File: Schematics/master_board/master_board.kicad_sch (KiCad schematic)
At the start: 9 parts

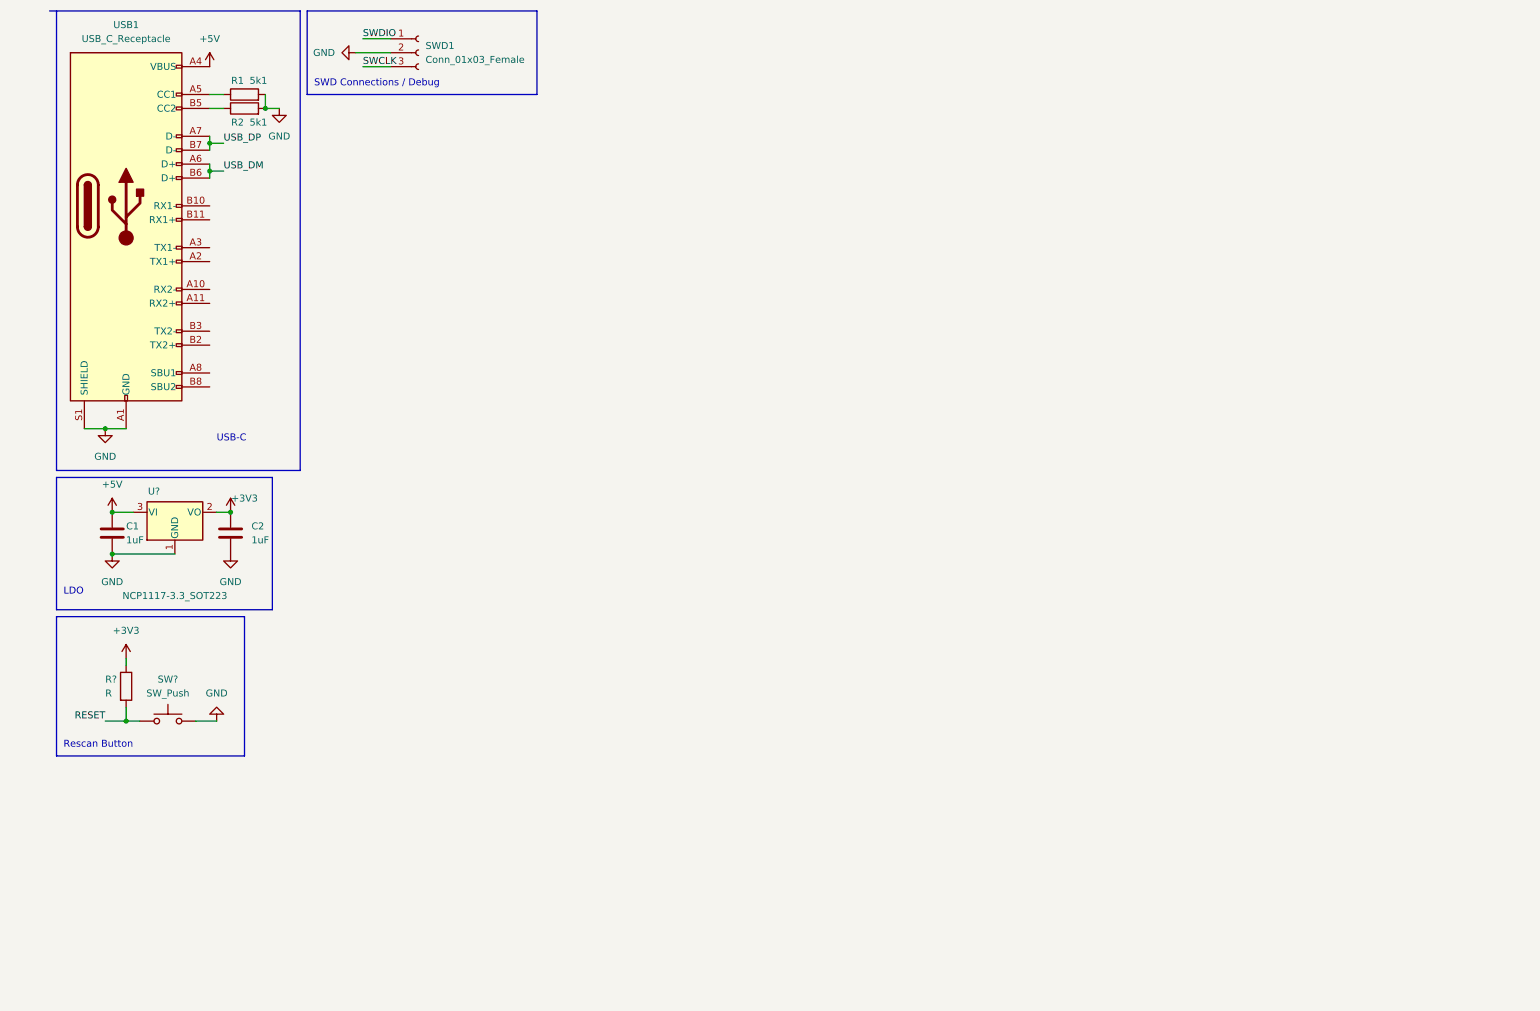
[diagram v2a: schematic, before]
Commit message: Consolidated board segments into corresponding board schematic & annotated components
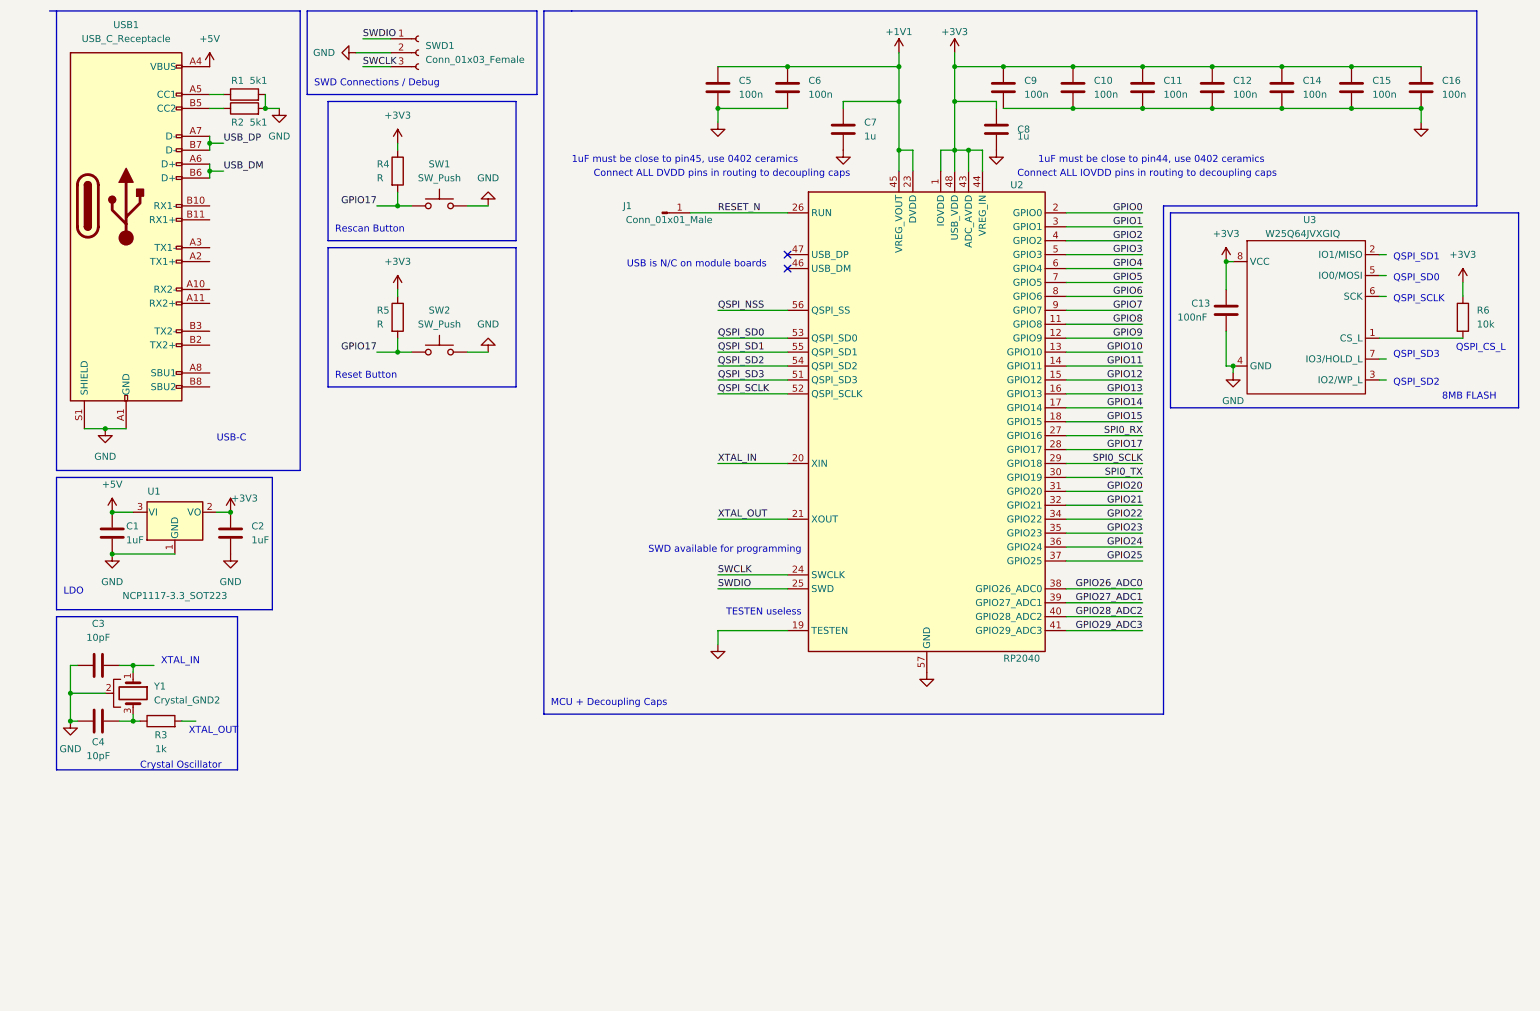
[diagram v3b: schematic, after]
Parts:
- added C10, C11, C12, C14, C15, C16, C5, C6, C9: 100n, symbol Device:C
- added C13: 100nF, symbol Device:C
- added C3, C4: 10pF, symbol Device:C
- added C7, C8: 1u, symbol Device:C
- added J1: Conn_01x01_Male, symbol Connector:Conn_01x01_Male
- added R3: 1k, symbol Device:R
- added R5: R, symbol Device:R
- added R6: 10k, symbol Device:R
- added SW2: SW_Push, symbol Switch:SW_Push
- added U2: RP2040, Package_DFN_QFN:QFN-56-1EP_7x7mm_P0.4mm_EP3.2x3.2mm, symbol MCU_RaspberryPi:RP2040
- added U3: W25Q64JVXGIQ, symbol Flash_Memory:W25Q64JVXGIQ
- added Y1: Crystal_GND2, symbol Device:Crystal_GND2
- gave numbers to parts that had none: 3
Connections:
- net +3V3: now also C10.1, C11.1, C12.1, C13.1, C14.1, C15.1, C16.1, C8.1, C9.1, R5.1, R6.1, U2.1 (IOVDD), U2.10 (IOVDD), U2.22 (IOVDD), U2.33 (IOVDD), U2.42 (IOVDD), U2.43 (ADC_AVDD), U2.44 (VREG_IN), U2.48 (USB_VDD), U2.49 (IOVDD), U3.8 (VCC)
- net GND: now also C10.2, C11.2, C12.2, C13.2, C14.2, C15.2, C16.2, C3.1, C4.1, C5.2, C6.2, C7.2, C8.2, C9.2, SW2.2, U2.19 (TESTEN), U2.57 (GND), U3.4 (GND), Y1.2
- net SWCLK: now also U2.24 (SWCLK)
- net SWDIO: now also U2.25 (SWD)
- net RESET renamed GPIO17
- net GPIO17: now also R5.2, SW2.1, U2.28 (GPIO17)
- new net: C4.2, R3.1, Y1.3
- new net: R6.2, U3.1 (CS_L)
- new net: C3.2, Y1.1
- new net +1V1: C5.1, C6.1, C7.1, U2.23 (DVDD), U2.45 (VREG_VOUT), U2.50 (DVDD)
- new net GPIO0: U2.2 (GPIO0)
- new net GPIO1: U2.3 (GPIO1)
- new net GPIO10: U2.13 (GPIO10)
- new net GPIO11: U2.14 (GPIO11)
- new net GPIO12: U2.15 (GPIO12)
- new net GPIO13: U2.16 (GPIO13)
- new net GPIO14: U2.17 (GPIO14)
- new net GPIO15: U2.18 (GPIO15)
- new net GPIO2: U2.4 (GPIO2)
- new net GPIO20: U2.31 (GPIO20)
- new net GPIO21: U2.32 (GPIO21)
- new net GPIO22: U2.34 (GPIO22)
- new net GPIO23: U2.35 (GPIO23)
- new net GPIO24: U2.36 (GPIO24)
- new net GPIO25: U2.37 (GPIO25)
- new net GPIO26_ADC0: U2.38 (GPIO26_ADC0)
- new net GPIO27_ADC1: U2.39 (GPIO27_ADC1)
- new net GPIO28_ADC2: U2.40 (GPIO28_ADC2)
- new net GPIO29_ADC3: U2.41 (GPIO29_ADC3)
- new net GPIO3: U2.5 (GPIO3)
- new net GPIO4: U2.6 (GPIO4)
- new net GPIO5: U2.7 (GPIO5)
- new net GPIO6: U2.8 (GPIO6)
- new net GPIO7: U2.9 (GPIO7)
- new net GPIO8: U2.11 (GPIO8)
- new net GPIO9: U2.12 (GPIO9)
- new net QSPI_NSS: U2.56 (QSPI_SS)
- new net QSPI_SCLK: U2.52 (QSPI_SCLK)
- new net QSPI_SD0: U2.53 (QSPI_SD0)
- new net QSPI_SD1: U2.55 (QSPI_SD1)
- new net QSPI_SD2: U2.54 (QSPI_SD2)
- new net QSPI_SD3: U2.51 (QSPI_SD3)
- new net RESET_N: J1.1 (Pin_1), U2.26 (RUN)
- new net SPI0_RX: U2.27 (GPIO16)
- new net SPI0_SCLK: U2.29 (GPIO18)
- new net SPI0_TX: U2.30 (GPIO19)
- new net XTAL_IN: U2.20 (XIN)
- new net XTAL_OUT: U2.21 (XOUT)
- no-connect marks 0 -> 2
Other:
- note added: "1uF must be close to pin44, use 0402 ceramics"
- note added: "1uF must be close to pin45, use 0402 ceramics"
- note added: "8MB FLASH"
- note added: "Connect ALL DVDD pins in routing to decoupling caps"
- note added: "Connect ALL IOVDD pins in routing to decoupling caps"
- note added: "Crystal Oscillator"
- note added: "MCU + Decoupling Caps"
- note added: "QSPI_CS_L"
- note added: "QSPI_SCLK"
- note added: "QSPI_SD0"
- note added: "QSPI_SD1"
- note added: "QSPI_SD2"
- note added: "QSPI_SD3"
- note added: "Reset Button"
- note added: "SWD available for programming"
- note added: "TESTEN useless"
- note added: "USB is N/C on module boards"
- note added: "XTAL_IN"
- note added: "XTAL_OUT"
- moved on the sheet: R4, SW1

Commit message: Fixed oscillator and flash labels
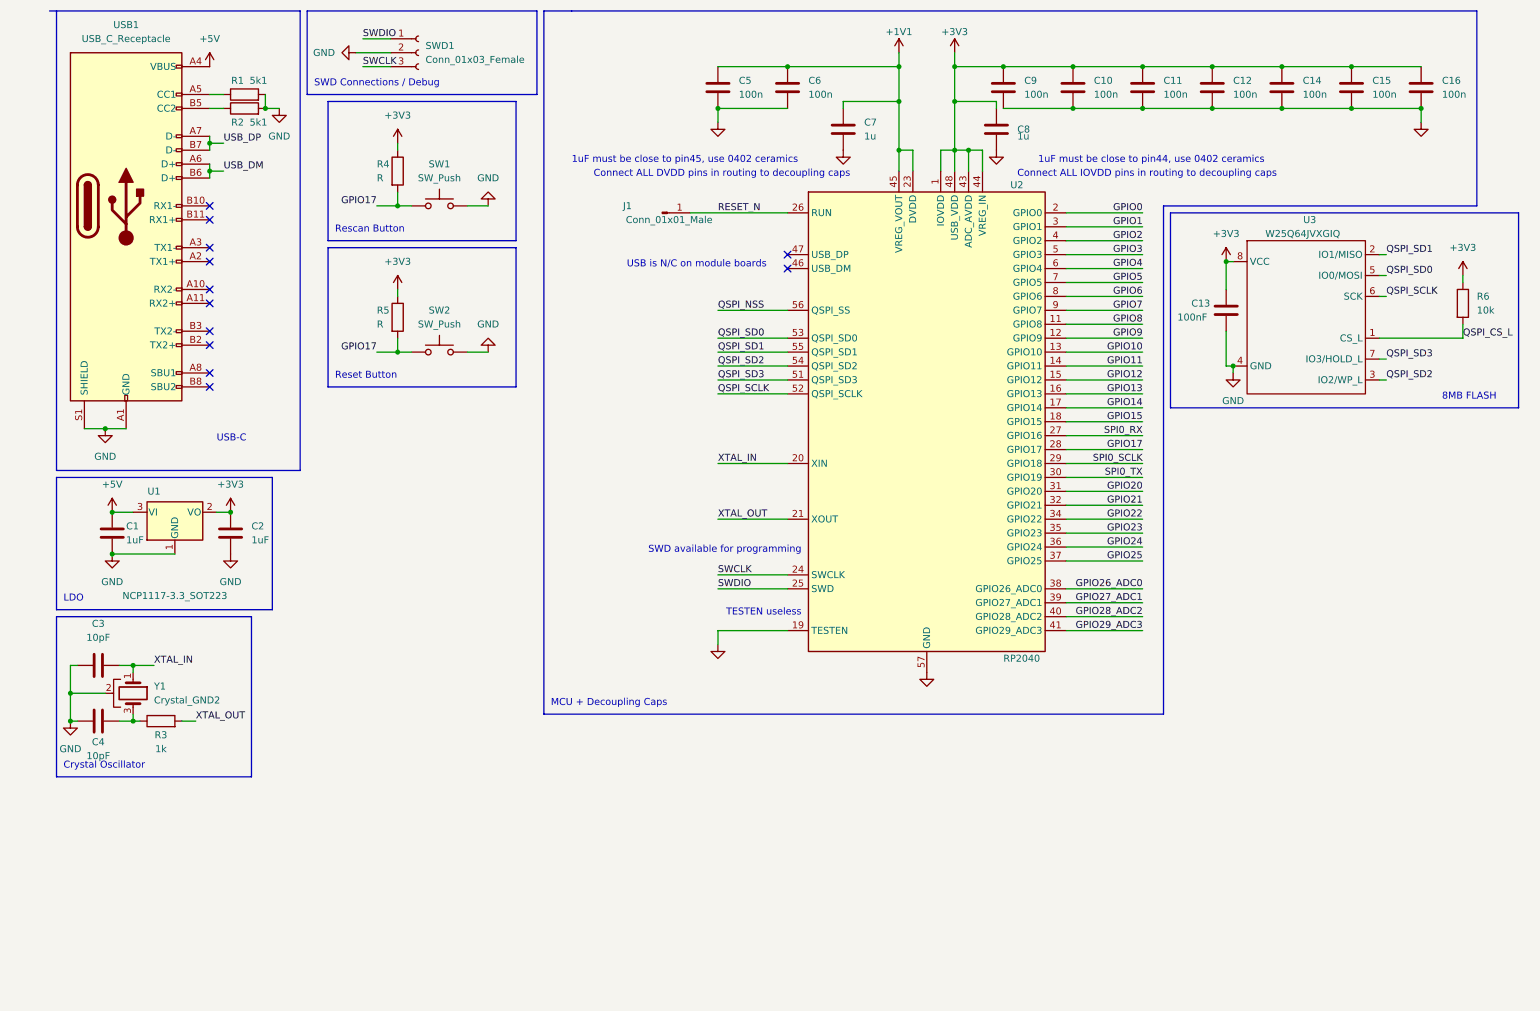
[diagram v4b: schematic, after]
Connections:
- net QSPI_SCLK: now also U3.6 (SCK)
- net QSPI_SD0: now also U3.5 (IO0/MOSI)
- net QSPI_SD1: now also U3.2 (IO1/MISO)
- net QSPI_SD2: now also U3.3 (IO2/WP_L)
- net QSPI_SD3: now also U3.7 (IO3/HOLD_L)
- net XTAL_IN: now also C3.2, Y1.1
- net XTAL_OUT: now also R3.2
- net QSPI_CS_L: now reaches R6.2, U3.1 (CS_L)
- no-connect marks 2 -> 12
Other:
- note removed: "QSPI_CS_L"
- note removed: "QSPI_SCLK"
- note removed: "QSPI_SD0"
- note removed: "QSPI_SD1"
- note removed: "QSPI_SD2"
- note removed: "QSPI_SD3"
- note removed: "XTAL_IN"
- note removed: "XTAL_OUT"
- moved on the sheet: R6
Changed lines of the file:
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@@
   (junction (at 187.96 24.13) (diameter 0) (color 0 0 0 0)
   )
+  (no_connect (at 43.18 74.93))
+  (no_connect (at 43.18 82.55))
   (no_connect (at 148.59 60.96))
+  (no_connect (at 43.18 52.07))
+  (no_connect (at 43.18 80.01))
+  (no_connect (at 43.18 59.69))
+  (no_connect (at 43.18 67.31))
+  (no_connect (at 43.18 57.15))
+  (no_connect (at 43.18 49.53))
+  (no_connect (at 43.18 64.77))
+  (no_connect (at 43.18 72.39))
   (no_connect (at 148.59 58.42))
   (wire (pts (xy 200.66 31.75) (xy 187.96 31.75))
@@
     (stroke (width 0) (type default) (color 0 0 0 0))
   )
-  (polyline (pts (xy 15.24 152.4) (xy 48.26 152.4))
+  (polyline (pts (xy 15.24 153.67) (xy 50.8 153.67))
     (stroke (width 0) (type default) (color 0 0 0 0))
   )
@@
     (stroke (width 0) (type default) (color 0 0 0 0))
   )
-  (polyline (pts (xy 15.24 124.46) (xy 15.24 152.4))
+  (polyline (pts (xy 15.24 124.46) (xy 15.24 153.67))
     (stroke (width 0) (type default) (color 0 0 0 0))
   )
@@
     (stroke (width 0) (type default) (color 0 0 0 0))
   )
-  (polyline (pts (xy 48.26 124.46) (xy 15.24 124.46))
+  (polyline (pts (xy 50.8 124.46) (xy 15.24 124.46))
     (stroke (width 0) (type default) (color 0 0 0 0))
   )
@@
     (stroke (width 0) (type default) (color 0 0 0 0))
   )
-  (polyline (pts (xy 48.26 152.4) (xy 48.26 124.46))
+  (polyline (pts (xy 50.8 153.67) (xy 50.8 124.46))
     (stroke (width 0) (type default) (color 0 0 0 0))
   )
@@
     (stroke (width 0) (type default) (color 0 0 0 0))
   )
+  (wire (pts (xy 256.54 73.66) (xy 271.78 73.66))
+    (stroke (width 0) (type default) (color 0 0 0 0))
+  )
   (wire (pts (xy 135.89 31.75) (xy 135.89 34.29))
     (stroke (width 0) (type default) (color 0 0 0 0))
@@
     (stroke (width 0) (type default) (color 0 0 0 0))
   )
+  (wire (pts (xy 271.78 71.12) (xy 271.78 73.66))
+    (stroke (width 0) (type default) (color 0 0 0 0))
+  )
   (wire (pts (xy 186.69 31.75) (xy 186.69 30.48))
     (stroke (width 0) (type default) (color 0 0 0 0))
@@
     (stroke (width 0) (type default) (color 0 0 0 0))
   )
-  (wire (pts (xy 271.78 66.04) (xy 271.78 63.5))
-    (stroke (width 0) (type default) (color 0 0 0 0))
-  )
   (polyline (pts (xy 64.77 30.48) (xy 99.06 30.48))
     (stroke (width 0) (type default) (color 0 0 0 0))
@@
     (stroke (width 0) (type default) (color 0 0 0 0))
   )
+  (wire (pts (xy 271.78 62.23) (xy 271.78 63.5))
+    (stroke (width 0) (type default) (color 0 0 0 0))
+  )
   (wire (pts (xy 135.89 116.84) (xy 148.59 116.84))
     (stroke (width 0) (type default) (color 0 0 0 0))
@@
     (stroke (width 0) (type default) (color 0 0 0 0))
   )
-  (wire (pts (xy 256.54 73.66) (xy 271.78 73.66))
-    (stroke (width 0) (type default) (color 0 0 0 0))
-  )
   (polyline (pts (xy 274.32 13.97) (xy 274.32 49.53))
     (stroke (width 0) (type default) (color 0 0 0 0))
@@
     (stroke (width 0) (type default) (color 0 0 0 0))
   )
-  (text "XTAL_IN" (at 34.29 133.35 0)
-    (effects (font (size 1.27 1.27)) (justify left bottom))
-  )
   (text "1uF must be close to pin45, use 0402 ceramics" (at 109.22 41.91 0)
-    (effects (font (size 1.27 1.27)) (justify left bottom))
-  )
-  (text "QSPI_SD3" (at 259.08 77.47 0)
     (effects (font (size 1.27 1.27)) (justify left bottom))
   )
@@
     (effects (font (size 1.27 1.27)) (justify left bottom))
   )
-  (text "QSPI_SD2" (at 259.08 82.55 0)
-    (effects (font (size 1.27 1.27)) (justify left bottom))
-  )
-  (text "Crystal Oscillator" (at 30.48 152.4 0)
+  (text "Crystal Oscillator" (at 16.51 152.4 0)
     (effects (font (size 1.27 1.27)) (justify left bottom))
   )
@@
     (effects (font (size 1.27 1.27)) (justify left bottom))
   )
-  (text "LDO" (at 16.51 120.65 0)
+  (text "LDO" (at 16.51 121.92 0)
     (effects (font (size 1.27 1.27)) (justify left bottom))
   )
@@
     (effects (font (size 1.27 1.27)) (justify right bottom))
   )
-  (text "XTAL_OUT" (at 39.37 146.05 0)
-    (effects (font (size 1.27 1.27)) (justify left bottom))
-  )
   (text "8MB FLASH\n" (at 267.97 85.09 0)
     (effects (font (size 1.27 1.27)) (justify left bottom))
   )
-  (text "QSPI_SD0" (at 259.08 63.5 0)
-    (effects (font (size 1.27 1.27)) (justify left bottom))
-  )
-  (text "QSPI_SD1" (at 259.08 59.69 0)
-    (effects (font (size 1.27 1.27)) (justify left bottom))
-  )
   (text "MCU + Decoupling Caps" (at 105.41 140.97 0)
     (effects (font (size 1.27 1.27)) (justify left bottom))
   )
-  (text "QSPI_SCLK" (at 259.08 67.31 0)
-    (effects (font (size 1.27 1.27)) (justify left bottom))
-  )
-  (text "QSPI_CS_L" (at 270.51 76.2 0)
-    (effects (font (size 1.27 1.27)) (justify left bottom))
-  )
   (label "GPIO6" (at 213.36 66.04 180)
     (effects (font (size 1.27 1.27)) (justify right bottom))
@@
     (effects (font (size 1.27 1.27)) (justify left bottom))
   )
+  (label "QSPI_SD0" (at 257.81 62.23 0)
+    (effects (font (size 1.27 1.27)) (justify left bottom))
+  )
   (label "GPIO8" (at 213.36 71.12 180)
     (effects (font (size 1.27 1.27)) (justify right bottom))
@@
     (effects (font (size 1.27 1.27)) (justify right bottom))
   )
+  (label "QSPI_SD3" (at 257.81 77.47 0)
+    (effects (font (size 1.27 1.27)) (justify left bottom))
+  )
   (label "SWDIO" (at 135.89 119.38 0)
     (effects (font (size 1.27 1.27)) (justify left bottom))
@@
     (effects (font (size 1.27 1.27)) (justify left bottom))
   )
+  (label "QSPI_SD2" (at 257.81 81.28 0)
+    (effects (font (size 1.27 1.27)) (justify left bottom))
+  )
   (label "XTAL_IN" (at 135.89 96.52 0)
     (effects (font (size 1.27 1.27)) (justify left bottom))
@@
     (effects (font (size 1.27 1.27)) (justify right bottom))
   )
+  (label "QSPI_CS_L" (at 271.78 73.66 0)
+    (effects (font (size 1.27 1.27)) (justify left bottom))
+  )
   (label "QSPI_SCLK" (at 135.89 83.82 0)
     (effects (font (size 1.27 1.27)) (justify left bottom))
@@
     (effects (font (size 1.27 1.27)) (justify left bottom))
   )
+  (label "XTAL_IN" (at 33.02 133.35 0)
+    (effects (font (size 1.27 1.27)) (justify left bottom))
+  )
   (label "SWDIO" (at 71.12 19.05 0)
     (effects (font (size 1.27 1.27)) (justify left bottom))
@@
     (effects (font (size 1.27 1.27)) (justify right bottom))
   )
+  (label "QSPI_SD1" (at 257.81 58.42 0)
+    (effects (font (size 1.27 1.27)) (justify left bottom))
+  )
   (label "GPIO27_ADC1" (at 213.36 121.92 180)
     (effects (font (size 1.27 1.27)) (justify right bottom))
@@
   (label "GPIO24" (at 213.36 111.76 180)
     (effects (font (size 1.27 1.27)) (justify right bottom))
+  )
+  (label "QSPI_SCLK" (at 257.81 66.04 0)
+    (effects (font (size 1.27 1.27)) (justify left bottom))
+  )
+  (label "XTAL_OUT" (at 40.64 143.51 0)
+    (effects (font (size 1.27 1.27)) (justify left bottom))
   )
   (label "GPIO26_ADC0" (at 213.36 119.38 180)
@@
       (effects (font (size 1.27 1.27)) hide)
     )
-    (property "Value" "+3V3" (id 1) (at 49.53 102.87 0))
+    (property "Value" "+3V3" (id 1) (at 46.99 100.33 0))
     (property "Footprint" "" (id 2) (at 46.99 105.41 0)
       (effects (font (size 1.27 1.27)) hide)
@@
     (pin "1")
   )
-  (symbol (lib_id "power:+3V3") (at 271.78 63.5 0) (unit 1)
-    (in_bom yes) (on_board yes) (fields_autoplaced)
-    (property "Reference" "#PWR024" (id 0) (at 271.78 67.31 0)
-      (effects (font (size 1.27 1.27)) hide)
-    )
-    (property "Value" "+3V3" (id 1) (at 271.78 58.42 0))
-    (property "Footprint" "" (id 2) (at 271.78 63.5 0)
-      (effects (font (size 1.27 1.27)) hide)
-    )
-    (property "Datasheet" "" (id 3) (at 271.78 63.5 0)
+  (symbol (lib_id "power:+3V3") (at 271.78 62.23 0) (unit 1)
+    (in_bom yes) (on_board yes) (fields_autoplaced)
+    (property "Reference" "#PWR024" (id 0) (at 271.78 66.04 0)
+      (effects (font (size 1.27 1.27)) hide)
+    )
+    (property "Value" "+3V3" (id 1) (at 271.78 57.15 0))
+    (property "Footprint" "" (id 2) (at 271.78 62.23 0)
+      (effects (font (size 1.27 1.27)) hide)
+    )
+    (property "Datasheet" "" (id 3) (at 271.78 62.23 0)
       (effects (font (size 1.27 1.27)) hide)
     )
@@
     (pin "2")
   )
-  (symbol (lib_id "Device:R") (at 271.78 69.85 0) (unit 1)
-    (in_bom yes) (on_board yes) (fields_autoplaced)
-    (property "Reference" "R6" (id 0) (at 274.32 68.5799 0)
-      (effects (font (size 1.27 1.27)) (justify left))
-    )
-    (property "Value" "10k" (id 1) (at 274.32 71.1199 0)
-      (effects (font (size 1.27 1.27)) (justify left))
-    )
-    (property "Footprint" "" (id 2) (at 270.002 69.85 90)
-      (effects (font (size 1.27 1.27)) hide)
-    )
-    (property "Datasheet" "~" (id 3) (at 271.78 69.85 0)
-      (effects (font (size 1.27 1.27)) hide)
-    )
+  (symbol (lib_id "Device:R") (at 271.78 67.31 0) (unit 1)
+    (in_bom yes) (on_board yes) (fields_autoplaced)
+    (property "Reference" "R6" (id 0) (at 274.32 66.0399 0)
+      (effects (font (size 1.27 1.27)) (justify left))
+    )
+    (property "Value" "10k" (id 1) (at 274.32 68.5799 0)
+      (effects (font (size 1.27 1.27)) (justify left))
+    )
+    (property "Footprint" "" (id 2) (at 270.002 67.31 90)
+      (effects (font (size 1.27 1.27)) hide)
+    )
+    (property "Datasheet" "~" (id 3) (at 271.78 67.31 0)
+      (effects (font (size 1.27 1.27)) hide)
+    )
